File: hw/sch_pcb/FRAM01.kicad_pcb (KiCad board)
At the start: 2 copper layers, 19.8 x 30 mm, 9 parts, among them IC1 CY15B108QN-40SXI, J2 HEADER_2x04, M1 HOLE M3, M2 HOLE M3, M3 HOLE, M4 HOLE

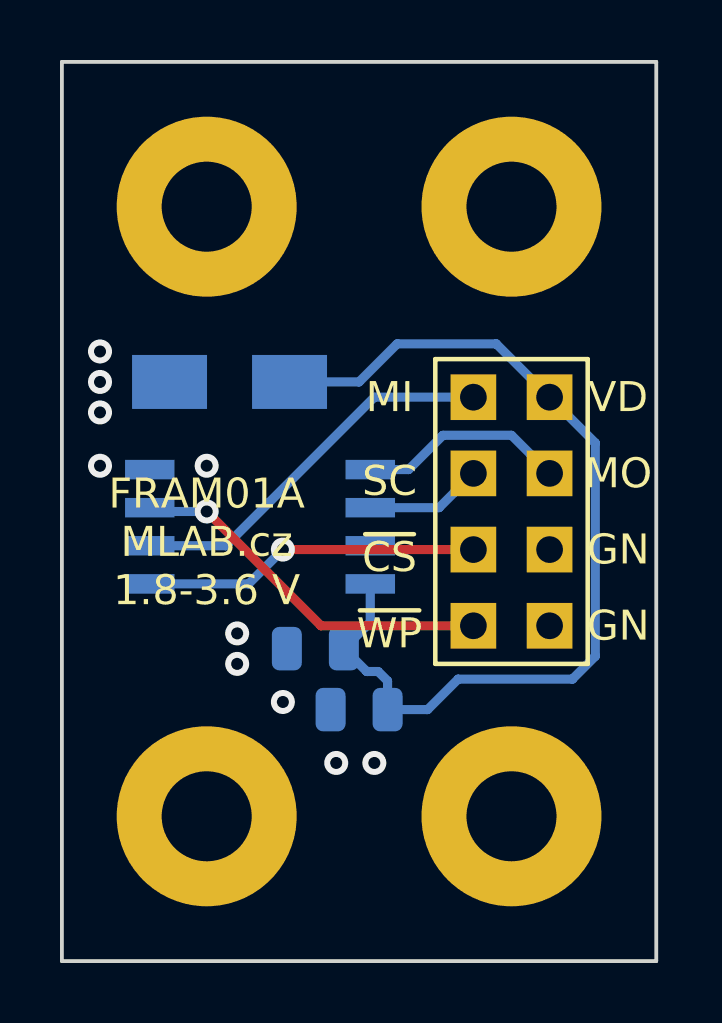
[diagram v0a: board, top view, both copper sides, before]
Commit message: power connection added, SPI connector changed
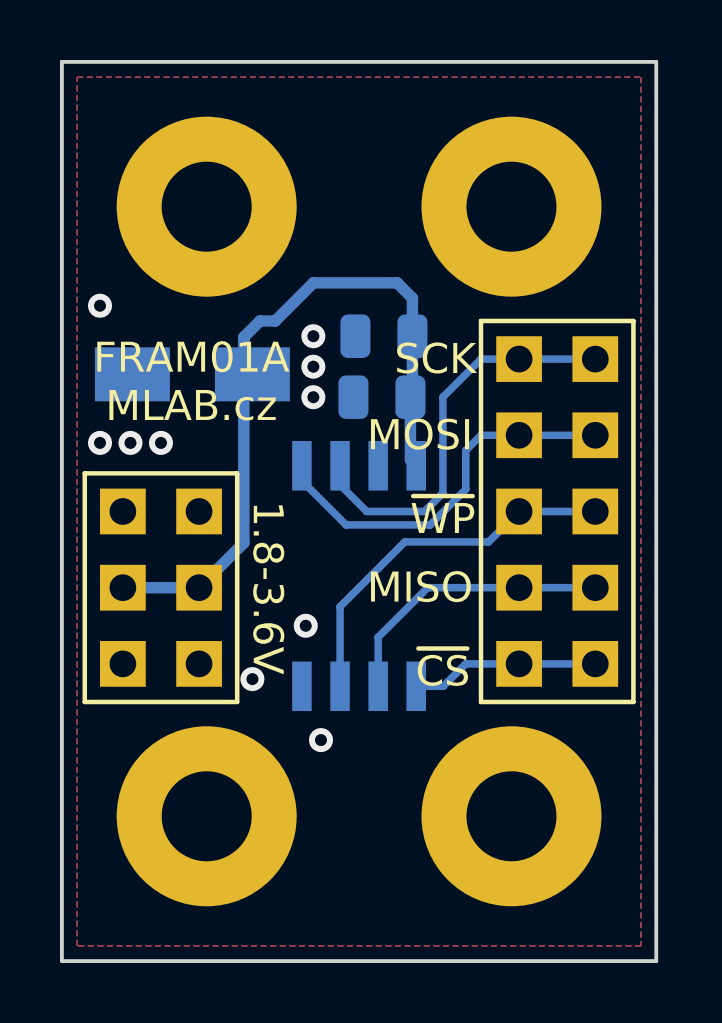
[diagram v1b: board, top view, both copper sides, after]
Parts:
- added J1: HEADER_2x03_PARALLEL, Mlab_Pin_Headers:Straight_2x03, F.Cu at (135.6, 88.9)
- J2: value HEADER_2x04 -> HEADER_2x05_PARALLEL; footprint Mlab_Pin_Headers:Straight_2x04 -> Mlab_Pin_Headers:Straight_2x05
- M1, M2: value HOLE M3 -> HOLE
- moved M3 22.7 mm to (137.2, 96.5)
- moved M2 20.3 mm to (137.2, 76.2)
- moved C1 12.5 mm to (143.1, 80.5)
- moved M1 10.2 mm to (147.3, 76.2)
- moved C2 8.67 mm to (143.0, 82.5)
- moved IC1 3.69 mm to (142.2, 88.5), turned to 90 degrees
- moved J2 1.52 mm to (148.8, 86.4)
- moved D1 1.26 mm to (136.7, 81.8)
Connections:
- C1 pad 1: +3.3V -> VDD
- C2 pad 1: +3.3V -> VDD
- D1 pad 1: +3.3V -> VDD
- IC1 pad 8: +3.3V -> VDD
- J2 pad 1: MISO -> SCK
- J2 pad 2: +3.3V -> SCK
- J2 pad 3: SCK -> MOSI
- J2 pad 5: ~{CS} -> ~{WP}
- J2 pad 6: GND -> ~{WP}
- J2 pad 7: ~{WP} -> MISO
- J2 pad 8: GND -> MISO
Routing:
- net +3.3V: track 32.2 -> 0.00 mm
- net VDD: track 0.00 -> 23.8 mm
- net SCK: track 3.91 -> 13.5 mm
- net MOSI: track 6.98 -> 12.9 mm
- net ~{CS}: track 11.3 -> 6.28 mm, vias 1 -> 0
- net MISO: track 12.8 -> 9.56 mm
- net ~{WP}: track 12.4 -> 12.5 mm, vias 1 -> 0
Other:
- board text added: "1.8-3.6V"
- board text added: "FRAM01A MLAB.cz"
- board text added: "MISO"
- board text added: "MOSI"
- board text added: "SCK"
- board text removed: "FRAM01A MLAB.cz 1.8-3.6 V"
- board text removed: "GN"
- board text removed: "MI"
- board text removed: "MO"
- board text removed: "SC"
- board text removed: "VD"
